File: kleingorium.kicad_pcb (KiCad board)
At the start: 2 copper layers, 126.5 x 72 mm, 41 parts, among them J1 4017 Pins, J10 VCC, J11 GND, J12 4046 Comp In, J2 4040 Output, J3 4040 Input, J4 4046 Out, J5 4046 Comp, J6 Select, J7 Output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

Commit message: renaming
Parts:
- removed C4, C5, C6, C7, C8: 100nF, Capacitor_THT:C_Disc_D3.0mm_W1.6mm_P2.50mm
- removed C9: 10uF, Capacitor_THT:CP_Radial_D5.0mm_P2.50mm
- added C10: 10uF, Capacitor_THT:CP_Radial_D5.0mm_P2.50mm, F.Cu at (90.3, 125.0)
- added C11: 100nF, Capacitor_THT:C_Disc_D3.0mm_W1.6mm_P2.50mm, F.Cu at (127.0, 103.2)
- added C12: 100nF, Capacitor_THT:C_Disc_D3.0mm_W1.6mm_P2.50mm, F.Cu at (152.8, 107.0)
- added C13: 100nF, Capacitor_THT:C_Disc_D3.0mm_W1.6mm_P2.50mm, F.Cu at (152.8, 126.1)
- added C14: 100nF, Capacitor_THT:C_Disc_D3.0mm_W1.6mm_P2.50mm, F.Cu at (125.7, 114.3)
- added C15: 100nF, Capacitor_THT:C_Disc_D3.0mm_W1.6mm_P2.50mm, F.Cu at (90.5, 103.2)
- added SW3: Chain, Button_Switch_THT:SW_E-Switch_EG1271_SPDT, F.Cu at (109.5, 120.9)
- Q1: footprint Package_TO_SOT_THT:TO-92_Inline -> Package_TO_SOT_THT:TO-92_Inline_Wide
- U1: value CD4053B -> 4046
- U2: value 4046 -> 4017
- U3: value 4017 -> CD4053B
- moved U3 68.0 mm to (129.7, 119.3), turned to 90 degrees
- moved U4 47.6 mm to (157.7, 112.3), turned to 90 degrees
- moved R8 42.5 mm to (161.9, 134.9), turned to 180 degrees
- moved R9 42.2 mm to (165.2, 134.9), turned to 0 degrees
- moved R3 40.5 mm to (119.5, 114.4)
- moved R4 40.1 mm to (119.5, 99.4)
- moved U5 34.8 mm to (132.5, 108.0), turned to 90 degrees
- moved U1 29.7 mm to (95.3, 108.3), turned to 90 degrees
- moved U2 29.3 mm to (156.9, 131.1), turned to 90 degrees
- moved C1 27.4 mm to (136.0, 122.5), turned to 0 degrees
- moved J2 26.7 mm to (153.1, 119.0)
- moved C2 19.9 mm to (130.3, 122.5), turned to 180 degrees
- moved J1 19.6 mm to (153.2, 144.7)
- moved J9 16.0 mm to (128.2, 126.5)
- moved R6 15.0 mm to (142.5, 140.5)
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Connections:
- C1 pad 1: Net-(U2-C1) -> Net-(U1-C1)
- C1 pad 2: Net-(U2-C2) -> Net-(U1-C2)
- C2 pad 1: Net-(U2-SigIn) -> Net-(U1-SigIn)
- J7 pad 2: /4053/C -> Net-(J7-Pin_2)
- Q1 pad 3: /4066/Cen -> /4066/Ben
- R1 pad 1: Net-(U1-INH) -> Net-(U3-INH)
- R11 pad 2: /4066/Cen -> /4066/Ben
- R3 pad 1: Net-(U2-Inh) -> Net-(U1-Inh)
- R4 pad 1: Net-(U2-R1) -> Net-(U1-R1)
- R5 pad 1: Net-(U2-PC2) -> Net-(U1-PC2)
- R5 pad 2: Net-(U2-VCOin) -> Net-(U1-VCOin)
- R5 pad 3: Net-(U2-VCOin) -> Net-(U1-VCOin)
- R6 pad 1: Net-(U2-VCOin) -> Net-(U1-VCOin)
- U1 pad 1: /4053/B1 -> unconnected-(U1-PCP-Pad1)
- U1 pad 10: /4053/Select -> unconnected-(U1-SFout-Pad10)
- U1 pad 11: /4053/Select -> Net-(U1-R1)
- U1 pad 12: /4017/Clock -> unconnected-(U1-R2-Pad12)
- U1 pad 13: /4046/SigIn -> Net-(U1-PC2)
- U1 pad 14: /4053/A -> Net-(U1-SigIn)
- U1 pad 15: /4053/B -> unconnected-(U1-ZOUT-Pad15)
- U1 pad 2: /4046/SigIn -> unconnected-(U1-PC1-Pad2)
- U1 pad 3: /4040/Q2 -> /4046/Comp
- U1 pad 4: /4053/C -> /4040/Clock
- U1 pad 5: /4040/Clock -> Net-(U1-Inh)
- U1 pad 6: Net-(U1-INH) -> Net-(U1-C1)
- U1 pad 7: GND -> Net-(U1-C2)
- U1 pad 9: /4053/Select -> Net-(U1-VCOin)
- U2 pad 1: unconnected-(U2-PCP-Pad1) -> /4017/Q5
- U2 pad 10: unconnected-(U2-SFout-Pad10) -> /4017/Q4
- U2 pad 11: Net-(U2-R1) -> /4017/Q9
- U2 pad 12: unconnected-(U2-R2-Pad12) -> /4017/Q10
- U2 pad 13: Net-(U2-PC2) -> /4017/ClockEnable
- U2 pad 14: Net-(U2-SigIn) -> /4017/Clock
- U2 pad 15: unconnected-(U2-ZOUT-Pad15) -> /4017/Reset
- U2 pad 2: unconnected-(U2-PC1-Pad2) -> /4017/Q1
- U2 pad 3: /4046/Comp -> /4017/Q0
- U2 pad 4: /4040/Clock -> /4017/Q2
- U2 pad 5: Net-(U2-Inh) -> /4017/Q6
- U2 pad 6: Net-(U2-C1) -> /4017/Q7
- U2 pad 7: Net-(U2-C2) -> /4017/Q3
- U2 pad 9: Net-(U2-VCOin) -> /4017/Q8
- U3 pad 1: /4017/Q5 -> /4053/B1
- U3 pad 10: /4017/Q4 -> /4053/Select
- U3 pad 11: /4017/Q9 -> /4053/Select
- U3 pad 12: /4017/Q10 -> /4017/Clock
- U3 pad 13: /4017/ClockEnable -> /4046/SigIn
- U3 pad 14: /4017/Clock -> /4053/A
- U3 pad 15: /4017/Reset -> /4053/B
- U3 pad 2: /4017/Q1 -> /4046/SigIn
- U3 pad 3: /4017/Q0 -> /4040/Q2
- U3 pad 4: /4017/Q2 -> /4053/C
- U3 pad 5: /4017/Q6 -> /4040/Clock
- U3 pad 6: /4017/Q7 -> Net-(U3-INH)
- U3 pad 7: /4017/Q3 -> GND
- U3 pad 9: /4017/Q8 -> /4053/Select
- U5 pad 1: /4066/A1 -> /4053/B1
- U5 pad 10: /4017/Clock -> /4066/D2
- U5 pad 11: /4040/Clock -> /4066/D1
- U5 pad 12: /4053/Select -> /4066/Den
- U5 pad 13: /4066/Aen -> /4053/Select
- U5 pad 2: /4066/A2 -> /4040/Q2
- U5 pad 3: /4066/B2 -> /4017/Clock
- U5 pad 4: /4066/B1 -> /4040/Clock
- U5 pad 8: /4053/B1 -> /4066/C1
- U5 pad 9: /4040/Q2 -> /4066/C2
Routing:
- net VCC: track 240.4 -> 0.00 mm, vias 3 -> 0
- net /4053/Select: track 116.3 -> 0.00 mm, vias 2 -> 0
- net /4017/Reset: track 109.8 -> 0.00 mm
- net /4040/Clock: track 113.7 -> 5.22 mm, vias 2 -> 0
- net /4017/Clock: track 103.2 -> 0.00 mm, vias 1 -> 0
- net /4053/B1: track 89.8 -> 0.00 mm
- net /4066/Cen: track 73.9 -> 0.00 mm, vias 1 -> 0
- net /4040/Q2: track 91.6 -> 24.0 mm
- net /4017/Q0: track 86.0 -> 19.7 mm, vias 1 -> 0
- net /4046/Comp: track 57.7 -> 0.00 mm, vias 1 -> 0
- net Net-(U2-VCOin): track 52.0 -> 0.00 mm
- net /4046/SigIn: track 48.6 -> 0.00 mm
- net /4053/A: track 37.1 -> 0.00 mm
- net /4053/C: track 35.5 -> 0.00 mm
- net Net-(U2-PC2): track 35.5 -> 0.00 mm
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- added copper zone on F.Cu, net VCC
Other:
- board size 126.5 x 72 mm -> 100 x 100 mm
- board text added: "4 0 1 7"
- board text added: "4017 Fdbk"
- board text added: "4046 CmpIn"
- board text added: "4053"
- board text added: "Chain"
- board text added: "Cmp"
- board text added: "CmpIn"
- board text removed: "4 0 5 3"
- board text removed: "4017"
- board text removed: "4017 Feedback"
- board text removed: "4046 CompIn"
- board text removed: "Comp"
- board text removed: "CompIn"

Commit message: before main routing
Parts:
- moved R1 47.2 mm to (135.9, 124.0)
- moved C1 29.9 mm to (107.5, 113.5)
- moved R2 5.44 mm to (100.1, 113.5), turned to 180 degrees
- moved R4 4.00 mm to (119.5, 103.4)
- moved SW3 3.13 mm to (107.1, 122.9)
- moved R3 2.50 mm to (119.5, 116.9)
- moved R12 2.08 mm to (105.0, 118.0)
- moved Q1 1.74 mm to (98.0, 126.4)
- moved J12 1.50 mm to (144.5, 128.5)
- moved SW2 1.00 mm to (115.1, 130.4)
- moved J6 0.72 mm to (107.0, 137.0)
- moved C15 0.71 mm to (91.0, 103.8)
- moved U1 0.58 mm to (95.6, 108.8)
- moved R11 0.53 mm to (90.0, 116.5)
- moved C10 0.53 mm to (90.1, 125.5)
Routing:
- net /4040/Q2: track 24.0 -> 56.3 mm
- net /4017/Clock: track 0.00 -> 23.5 mm, vias 0 -> 1

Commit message: after main routing
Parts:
- moved R1 9.16 mm to (145.1, 124.0), turned to 180 degrees
- moved SW3 7.76 mm to (105.1, 130.4)
- moved R3 5.31 mm to (121.5, 112.0)
- moved J6 5.06 mm to (106.5, 142.0)
- moved C1 2.69 mm to (105.0, 112.5)
- moved Q1 2.50 mm to (96.5, 124.4)
- moved R4 2.12 mm to (118.0, 101.9)
- moved C14 2.03 mm to (127.0, 112.8)
- moved SW2 1.50 mm to (115.1, 128.9)
- moved J4 1.34 mm to (129.5, 133.8)
- moved J7 1.21 mm to (97.2, 133.0)
- moved C11 0.96 mm to (128.0, 103.2)
- moved R12 0.50 mm to (105.0, 118.5)
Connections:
- J7 pad 2: Net-(J7-Pin_2) -> /4053/C
- SW3 pad 2: Net-(J7-Pin_2) -> /4053/C
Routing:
- net /4053/Select: track 0.00 -> 135.1 mm
- net /4040/Clock: track 5.22 -> 128.0 mm, vias 0 -> 1
- net /4017/Reset: track 0.00 -> 97.9 mm, vias 0 -> 1
- net /4053/B1: track 0.00 -> 72.9 mm, vias 0 -> 1
- net /4053/C: track 0.00 -> 66.0 mm
- net Net-(U1-VCOin): track 0.00 -> 59.3 mm, vias 0 -> 1
- net /4066/Ben: track 0.00 -> 58.5 mm
- net /4046/Comp: track 0.00 -> 54.1 mm
- net /4053/A: track 0.00 -> 53.6 mm
- net Net-(U1-PC2): track 0.00 -> 49.6 mm, vias 0 -> 1
- net /4040/Q0: track 0.00 -> 45.0 mm
- net /4053/B: track 0.00 -> 44.7 mm, vias 0 -> 2
- net Net-(U1-SigIn): track 0.00 -> 43.7 mm
- net /4017/Q3: track 0.00 -> 40.9 mm
- net /4017/Q0: track 19.7 -> 56.5 mm
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
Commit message: after fixing errors
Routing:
- net GND: track 0.00 -> 113.8 mm, vias 0 -> 1
- net VCC: track 0.00 -> 24.5 mm, vias 0 -> 1

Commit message: fix errors
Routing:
- net GND: track 113.8 -> 117.4 mm, vias 1 -> 3
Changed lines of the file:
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@@
+	)
+	(segment
+		(start 170.5 109)
+		(end 168 106.5)
+		(width 0.2)
+		(layer "F.Cu")
+		(net 2)
 	)
 	(segment
@@
 		(net 2)
 	)
+	(via
+		(at 170.5 109)
+		(size 0.6)
+		(drill 0.3)
+		(layers "F.Cu" "B.Cu")
+		(free yes)
+		(net 2)
+	)
+	(via
+		(at 168 106.5)
+		(size 0.6)
+		(drill 0.3)
+		(layers "F.Cu" "B.Cu")
+		(net 2)
+	)

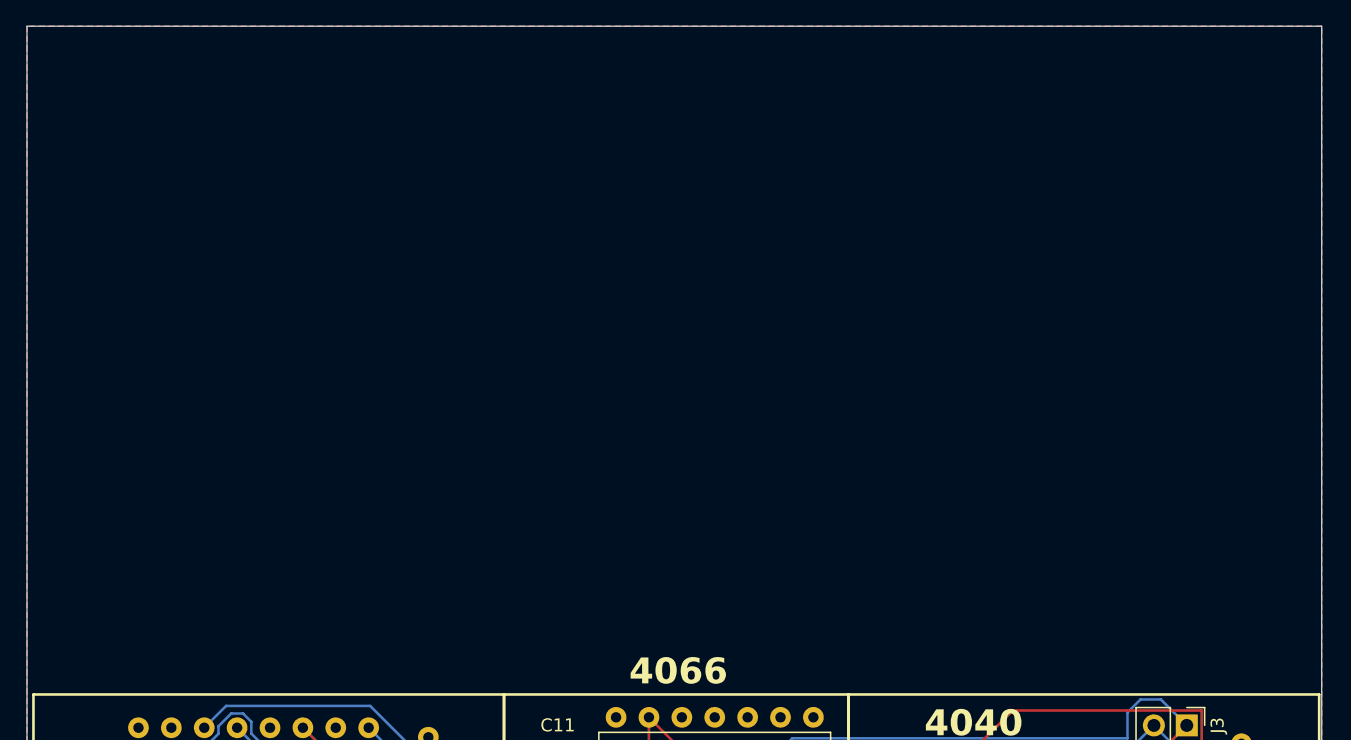
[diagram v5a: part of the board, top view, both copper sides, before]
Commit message: pcb placing doubling without routing
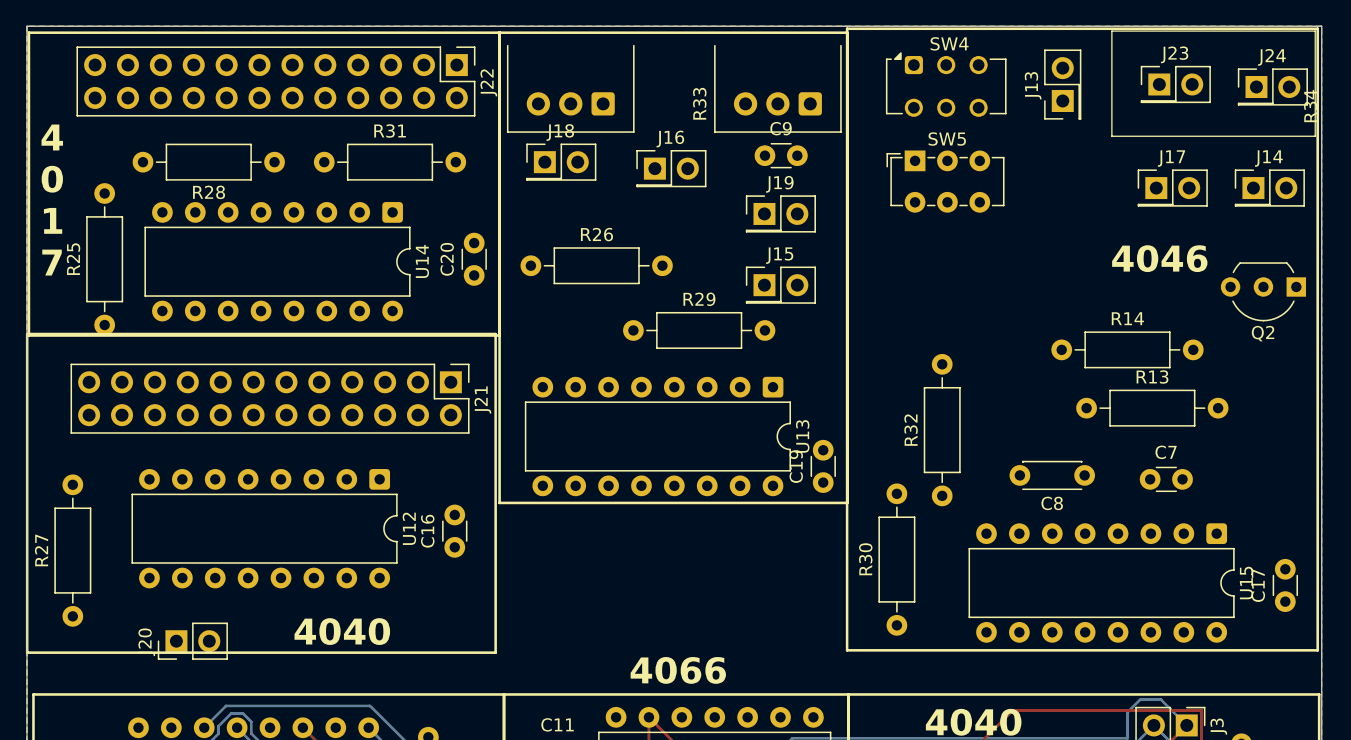
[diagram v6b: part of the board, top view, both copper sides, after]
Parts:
- added C16: 100nF, Capacitor_THT:C_Disc_D3.0mm_W1.6mm_P2.50mm, F.Cu at (120.0, 87.2)
- added C17: 100nF, Capacitor_THT:C_Disc_D3.0mm_W1.6mm_P2.50mm, F.Cu at (184.2, 91.4)
- added C19: 100nF, Capacitor_THT:C_Disc_D3.0mm_W1.6mm_P2.50mm, F.Cu at (148.5, 82.2)
- added C20: 100nF, Capacitor_THT:C_Disc_D3.0mm_W1.6mm_P2.50mm, F.Cu at (121.5, 66.2)
- added C7: 1uF, Capacitor_THT:C_Disc_D3.0mm_W1.6mm_P2.50mm, F.Cu at (173.8, 82.0)
- added C8: C1, Capacitor_THT:C_Disc_D4.3mm_W1.9mm_P5.00mm, F.Cu at (168.7, 81.7)
- added C9: 1uF, Capacitor_THT:C_Disc_D3.0mm_W1.6mm_P2.50mm, F.Cu at (144.0, 57.0)
- added J13: Select, Connector_PinHeader_2.54mm:PinHeader_2x01_P2.54mm_Vertical, F.Cu at (167.0, 52.8)
- added J14: Input, Connector_PinHeader_2.54mm:PinHeader_2x01_P2.54mm_Vertical, F.Cu at (181.7, 59.5)
- added J15: 4046 SigIn, Connector_PinHeader_2.54mm:PinHeader_2x01_P2.54mm_Vertical, F.Cu at (144.0, 67.0)
- added J16: 4046 Comp, Connector_PinHeader_2.54mm:PinHeader_2x01_P2.54mm_Vertical, F.Cu at (135.5, 58.0)
- added J17: Output, Connector_PinHeader_2.54mm:PinHeader_2x01_P2.54mm_Vertical, F.Cu at (174.2, 59.5)
- added J18: 4046 Comp In, Connector_PinHeader_2.54mm:PinHeader_2x01_P2.54mm_Vertical, F.Cu at (127.0, 57.5)
- added J19: 4046 Out, Connector_PinHeader_2.54mm:PinHeader_2x01_P2.54mm_Vertical, F.Cu at (144.0, 61.5)
- added J20: 4040 Input, Connector_PinHeader_2.54mm:PinHeader_1x02_P2.54mm_Vertical, F.Cu at (98.5, 94.5)
- added J21: 4040 Output, Connector_PinHeader_2.54mm:PinHeader_2x12_P2.54mm_Vertical, F.Cu at (119.7, 74.5)
- added J22: 4017 Pins, Connector_PinHeader_2.54mm:PinHeader_2x12_P2.54mm_Vertical, F.Cu at (120.2, 50.0)
- added J23: VCC, Connector_PinHeader_2.54mm:PinHeader_2x01_P2.54mm_Vertical, F.Cu at (174.5, 51.5)
- added J24: GND, Connector_PinHeader_2.54mm:PinHeader_2x01_P2.54mm_Vertical, F.Cu at (182.0, 51.7)
- added Q2: 2N3904, Package_TO_SOT_THT:TO-92_Inline_Wide, F.Cu at (185.0, 67.1)
- added R13: 100k, Resistor_THT:R_Axial_DIN0207_L6.3mm_D2.5mm_P10.16mm_Horizontal, F.Cu at (168.8, 76.5)
- added R14: 10k, Resistor_THT:R_Axial_DIN0207_L6.3mm_D2.5mm_P10.16mm_Horizontal, F.Cu at (166.9, 72.0)
- added R25: 100K, Resistor_THT:R_Axial_DIN0207_L6.3mm_D2.5mm_P10.16mm_Horizontal, F.Cu at (93.0, 70.1)
- added R26: 100K, Resistor_THT:R_Axial_DIN0207_L6.3mm_D2.5mm_P10.16mm_Horizontal, F.Cu at (125.9, 65.5)
- added R27: 100K, Resistor_THT:R_Axial_DIN0207_L6.3mm_D2.5mm_P10.16mm_Horizontal, F.Cu at (90.5, 92.6)
- added R28: 100K, Resistor_THT:R_Axial_DIN0207_L6.3mm_D2.5mm_P10.16mm_Horizontal, F.Cu at (106.1, 57.5)
- added R29: 100K, Resistor_THT:R_Axial_DIN0207_L6.3mm_D2.5mm_P10.16mm_Horizontal, F.Cu at (133.8, 70.5)
- added R30: 100K, Resistor_THT:R_Axial_DIN0207_L6.3mm_D2.5mm_P10.16mm_Horizontal, F.Cu at (154.2, 93.3)
- added R31: 100K, Resistor_THT:R_Axial_DIN0207_L6.3mm_D2.5mm_P10.16mm_Horizontal, F.Cu at (110.0, 57.5)
- added R32: 100K, Resistor_THT:R_Axial_DIN0207_L6.3mm_D2.5mm_P10.16mm_Horizontal, F.Cu at (157.7, 83.3)
- added R33: R5, Potentiometer_THT:Potentiometer_Alps_RK097_Single_Horizontal, F.Cu at (147.5, 53.0)
- added R34: R6, Potentiometer_THT:Potentiometer_Alps_RK097_Single_Horizontal, F.Cu at (131.5, 53.0)
- added SW4: 4017 Feedback, Button_Switch_THT:SW_CK_JS202011CQN_DPDT_Straight, F.Cu at (155.5, 50.0)
- added SW5: 4046 CompIn, Button_Switch_THT:SW_E-Switch_EG1271_SPDT, F.Cu at (155.6, 57.4)
- added U12: 4040, Package_DIP:DIP-16_W7.62mm, F.Cu at (114.2, 82.0)
- added U13: CD4053B, Package_DIP:DIP-16_W7.62mm, F.Cu at (144.6, 74.9)
- added U14: 4017, Package_DIP:DIP-16_W7.62mm, F.Cu at (115.2, 61.4)
- added U15: 4046, Package_DIP:DIP-16_W7.62mm, F.Cu at (178.9, 86.2)
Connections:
- SW3 pad 1: unconnected-(SW3-A-Pad1) -> /4055/A
- U5 pad 10: /4066/D2 -> /4042/Q2
- U5 pad 11: /4066/D1 -> /4055/B1
- U5 pad 12: /4066/Den -> /4055/Select
- U5 pad 8: /4066/C1 -> /4042/Clock
- U5 pad 9: /4066/C2 -> /4019/Clock

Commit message: final version v1
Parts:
- added C18: 10uF, Capacitor_THT:CP_Radial_D5.0mm_P2.50mm, F.Cu at (183.5, 69.9)
- moved R26 49.9 mm to (173.5, 80.7)
- moved SW3 42.3 mm to (126.0, 93.7)
- moved C7 32.2 mm to (143.3, 71.7)
- moved R14 17.6 mm to (183.6, 77.7), turned to 180 degrees
- moved C9 14.9 mm to (129.1, 57.9), turned to 180 degrees
- moved J18 8.43 mm to (129.1, 65.7), turned to 180 degrees
- moved SW5 8.38 mm to (158.5, 65.3), turned to 180 degrees
- moved Q2 8.35 mm to (177.1, 69.8)
- moved SW4 5.71 mm to (158.6, 54.8), turned to 180 degrees
- moved R32 5.71 mm to (152.1, 82.2)
- moved R29 5.34 mm to (128.5, 70.2)
- moved J16 2.88 mm to (136.6, 60.7), turned to 180 degrees
- moved R28 2.86 mm to (108.4, 59.3)
- moved J17 2.71 mm to (176.4, 61.1), turned to 180 degrees
- moved J14 2.55 mm to (183.7, 61.1), turned to 180 degrees
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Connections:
- net /4019/Clock renamed /4017 2/Clock
- net /4019/ClockEnable renamed /4017 2/ClockEnable
- net /4019/Q0 renamed /4017 2/Q0
- net /4019/Q1 renamed /4017 2/Q1
- net /4019/Q10 renamed /4017 2/Q10
- net /4019/Q2 renamed /4017 2/Q2
- net /4019/Q3 renamed /4017 2/Q3
- net /4019/Q4 renamed /4017 2/Q4
- net /4019/Q5 renamed /4017 2/Q5
- net /4019/Q6 renamed /4017 2/Q6
- net /4019/Q7 renamed /4017 2/Q7
- net /4019/Q8 renamed /4017 2/Q8
- net /4019/Q9 renamed /4017 2/Q9
- net /4019/Reset renamed /4017 2/Reset
- net /4042/Clock renamed /4040 2/Clock
- net /4042/Q0 renamed /4040 2/Q0
- net /4042/Q1 renamed /4040 2/Q1
- net /4042/Q10 renamed /4040 2/Q10
- net /4042/Q11 renamed /4040 2/Q11
- net /4042/Q2 renamed /4040 2/Q2
- net /4042/Q3 renamed /4040 2/Q3
- net /4042/Q4 renamed /4040 2/Q4
- net /4042/Q5 renamed /4040 2/Q5
- net /4042/Q6 renamed /4040 2/Q6
- net /4042/Q7 renamed /4040 2/Q7
- net /4042/Q8 renamed /4040 2/Q8
- net /4042/Q9 renamed /4040 2/Q9
- net /4042/Reset renamed /4040 2/Reset
- net /4048/Comp renamed /4046 2/Comp
- net /4048/SigIn renamed /4046 2/SigIn
- net /4055/A renamed /4053 2/A
- net /4055/B renamed /4053 2/B
- net /4055/B1 renamed /4053 2/B1
- net /4055/C renamed /4053 2/C
- net /4055/Select renamed /4053 2/Select
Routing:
- net /4040 2/Clock: track 0.00 -> 148.5 mm, vias 0 -> 2
- net /4053 2/Select: track 0.00 -> 142.2 mm
- net GND: track 117.4 -> 242.3 mm, vias 3 -> 8
- net /4017 2/Reset: track 0.00 -> 97.9 mm, vias 0 -> 1
- net /4066/Cen: track 0.00 -> 91.1 mm, vias 0 -> 2
- net /4053 2/B1: track 0.00 -> 90.2 mm, vias 0 -> 2
- net /4017 2/Clock: track 0.00 -> 84.1 mm, vias 0 -> 3
- net /4040 2/Q2: track 0.00 -> 77.2 mm, vias 0 -> 1
- net /4053 2/A: track 0.00 -> 73.0 mm, vias 0 -> 1
- net /4053 2/C: track 0.00 -> 61.8 mm
- net Net-(U15-VCOin): track 0.00 -> 59.3 mm, vias 0 -> 1
- net /4017 2/Q0: track 0.00 -> 57.6 mm
- net VCC: track 24.5 -> 80.1 mm, vias 1 -> 2
- net /4046 2/Comp: track 0.00 -> 54.1 mm
- net Net-(U15-PC2): track 0.00 -> 49.6 mm, vias 0 -> 1
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
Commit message: final version v2
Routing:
- net /4053/C: track 100.8 -> 92.9 mm
- net /4053 2/C: track 61.8 -> 58.1 mm
- net /4066/Cen: track 91.1 -> 87.6 mm
- net /4017 2/ClockEnable: track 16.2 -> 15.1 mm
- net VCC: track 80.1 -> 79.6 mm
